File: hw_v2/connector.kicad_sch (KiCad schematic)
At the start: 22 parts, among them J1 Conn_02x24_Counter_Clockwise, J14 Conn_01x04, U11 L78M05ABDT-TR, U19 L78M05ABDT-TR, U25 74LVC2G17, U26 74LVC2G17, U8 AMS1117-3.3

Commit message: WIP v7
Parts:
- D37, U25: now in the parts list
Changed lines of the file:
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@@
 (kicad_sch
-	(version 20240101)
+	(version 20241004)
 	(generator "eeschema")
 	(generator_version "8.99")
@@
 		(shape input)
 		(at 264.16 82.55 0)
-		(fields_autoplaced yes)
 		(effects
 			(font
@@
 		(shape input)
 		(at 264.16 97.79 0)
-		(fields_autoplaced yes)
 		(effects
 			(font
@@
 		(shape input)
 		(at 264.16 90.17 0)
-		(fields_autoplaced yes)
 		(effects
 			(font
@@
 		(shape input)
 		(at 264.16 74.93 0)
-		(fields_autoplaced yes)
 		(effects
 			(font
@@
 		(unit 3)
 		(exclude_from_sim no)
-		(in_bom no)
+		(in_bom yes)
 		(on_board yes)
 		(dnp no)
@@
 		(at 149.86 40.005 0)
 		(unit 1)
-		(exclude_from_sim yes)
-		(in_bom no)
-		(on_board no)
+		(exclude_from_sim no)
+		(in_bom yes)
+		(on_board yes)
 		(dnp no)
 		(property "Reference" "#PWR0198"
@@
 		(at 143.51 34.29 270)
 		(unit 1)
-		(exclude_from_sim yes)
-		(in_bom no)
-		(on_board no)
+		(exclude_from_sim no)
+		(in_bom yes)
+		(on_board yes)
 		(dnp no)
 		(property "Reference" "D37"
@@
 		(at 251.46 82.55 0)
 		(unit 2)
-		(exclude_from_sim yes)
+		(exclude_from_sim no)
 		(in_bom yes)
 		(on_board yes)
@@
 		(at 143.51 22.225 0)
 		(unit 1)
-		(exclude_from_sim yes)
-		(in_bom no)
+		(exclude_from_sim no)
+		(in_bom yes)
 		(on_board yes)
 		(dnp no)
@@
 		(at 130.81 20.955 0)
 		(unit 1)
-		(exclude_from_sim yes)
-		(in_bom no)
-		(on_board no)
+		(exclude_from_sim no)
+		(in_bom yes)
+		(on_board yes)
 		(dnp no)
 		(property "Reference" "#PWR0199"

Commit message: hw v2
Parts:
- U26: footprint (none) -> Package_TO_SOT_SMD:SOT-363_SC-70-6
- U26: footprint (none) -> Package_TO_SOT_SMD:SOT-363_SC-70-6; now left out of the parts list
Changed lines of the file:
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@@
 			)
 		)
-		(property "Footprint" ""
+		(property "Footprint" "Package_TO_SOT_SMD:SOT-363_SC-70-6"
 			(at 250.19 147.32 0)
 			(effects
@@
 		(unit 1)
 		(exclude_from_sim no)
-		(in_bom yes)
+		(in_bom no)
 		(on_board yes)
 		(dnp no)
@@
 			)
 		)
-		(property "Footprint" ""
+		(property "Footprint" "Package_TO_SOT_SMD:SOT-363_SC-70-6"
 			(at 238.76 90.17 0)
 			(effects
@@
 			)
 		)
-		(property "Footprint" ""
+		(property "Footprint" "Package_TO_SOT_SMD:SOT-363_SC-70-6"
 			(at 251.46 97.79 0)
 			(effects

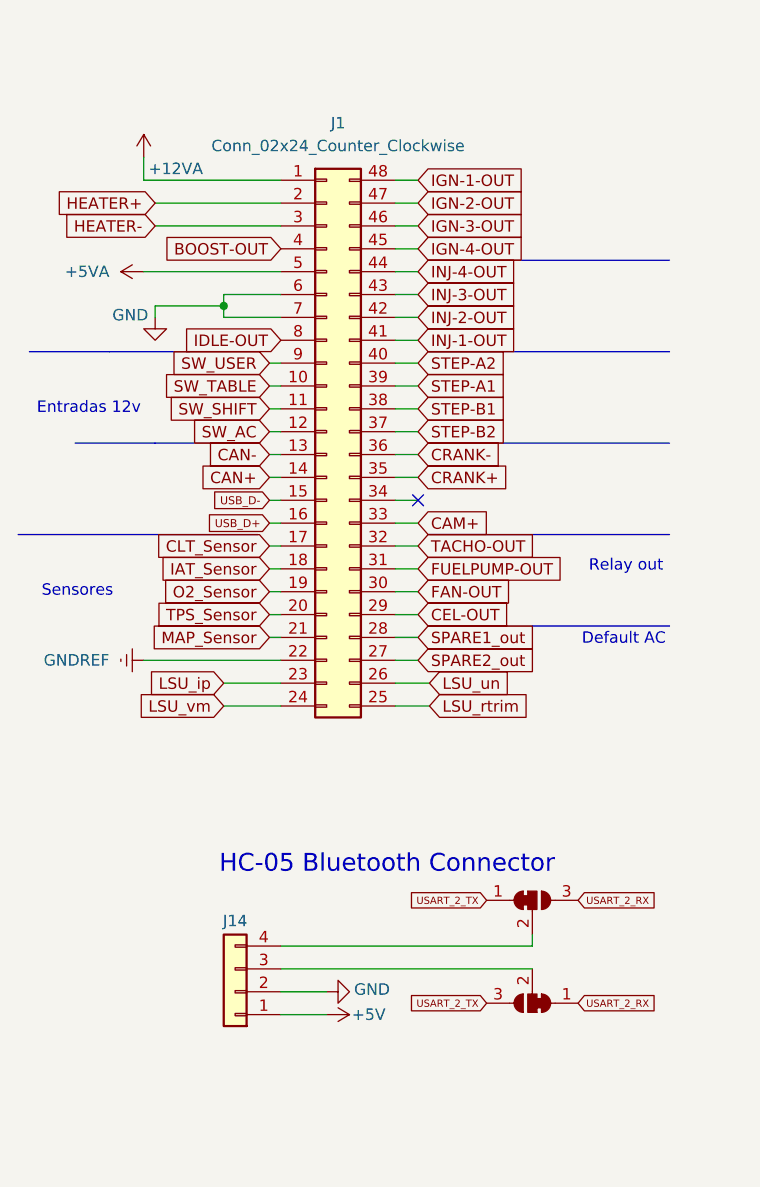
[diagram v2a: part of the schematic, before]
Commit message: fix LCSC codes
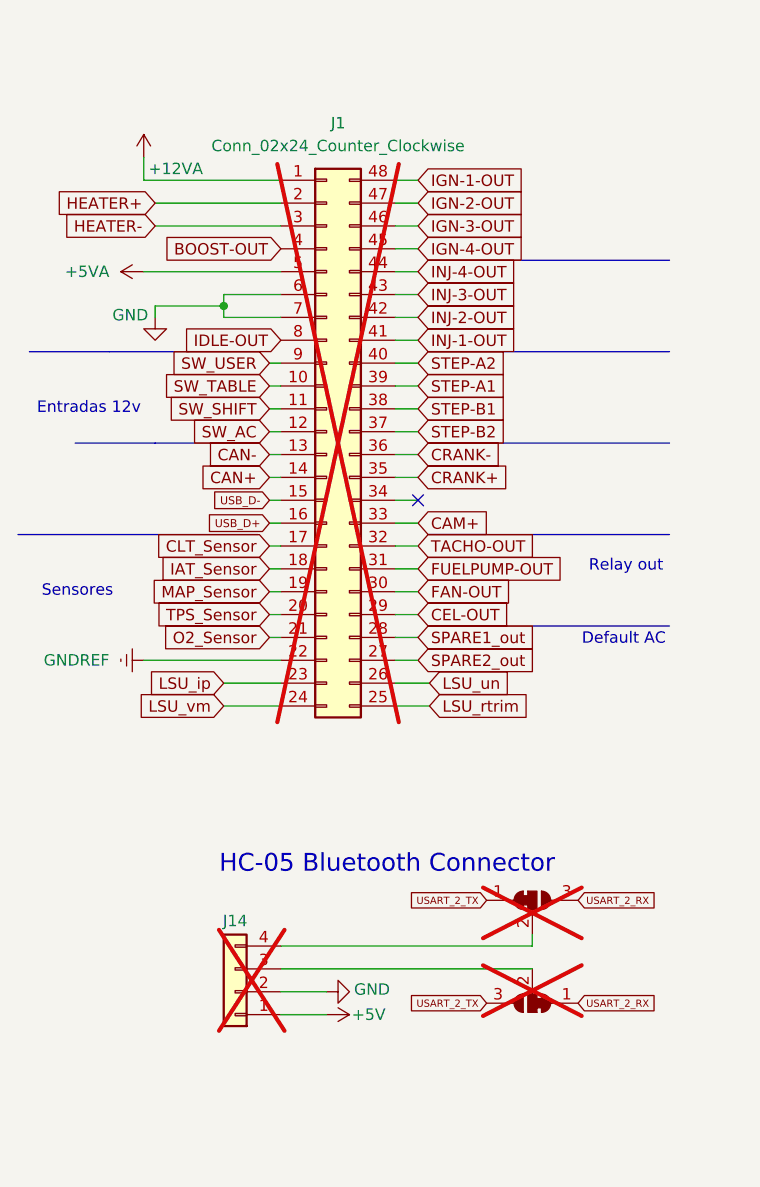
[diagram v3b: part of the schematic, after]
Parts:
- C51, C69, D17, RN7, U26: now in the parts list
- J1, JP10, JP9: now not fitted
- J14: now not fitted; now left out of the parts list
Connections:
- net MAP_Sensor: now also J1.19 (Pin_19); no longer J1.21 (Pin_21)
- net O2_Sensor: now also J1.21 (Pin_21); no longer J1.19 (Pin_19)
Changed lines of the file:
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@@
 	(global_label "MAP_Sensor"
 		(shape input)
-		(at 72.39 104.14 180)
+		(at 72.39 99.06 180)
 		(effects
 			(font
@@
 		)
 		(property "Intersheetrefs" "${INTERSHEET_REFS}"
-			(at 72.39 104.14 0)
+			(at 72.39 99.06 0)
 			(effects
 				(font
@@
 	(global_label "O2_Sensor"
 		(shape input)
-		(at 72.39 99.06 180)
+		(at 72.39 104.14 180)
 		(effects
 			(font
@@
 		)
 		(property "Intersheetrefs" "${INTERSHEET_REFS}"
-			(at 72.39 99.06 0)
+			(at 72.39 104.14 0)
 			(effects
 				(font
@@
 		(unit 3)
 		(exclude_from_sim no)
-		(in_bom no)
+		(in_bom yes)
 		(on_board yes)
 		(dnp no)
@@
 		(unit 1)
 		(exclude_from_sim no)
-		(in_bom no)
+		(in_bom yes)
 		(on_board yes)
 		(dnp no)
@@
 		(unit 1)
 		(exclude_from_sim no)
-		(in_bom no)
+		(in_bom yes)
 		(on_board yes)
 		(dnp no)
@@
 		(unit 1)
 		(exclude_from_sim no)
-		(in_bom no)
+		(in_bom yes)
 		(on_board yes)
 		(dnp no)
@@
 		(in_bom no)
 		(on_board yes)
-		(dnp no)
+		(dnp yes)
 		(property "Reference" "JP9"
 			(at 101.6 129.54 0)
@@
 		(unit 1)
 		(exclude_from_sim no)
-		(in_bom yes)
+		(in_bom no)
 		(on_board yes)
-		(dnp no)
+		(dnp yes)
 		(property "Reference" "J14"
 			(at 68.58 135.636 0)
@@
 		(in_bom no)
 		(on_board yes)
-		(dnp no)
+		(dnp yes)
 		(property "Reference" "J1"
 			(at 80.01 46.99 0)
@@
 		(in_bom no)
 		(on_board yes)
-		(dnp no)
+		(dnp yes)
 		(fields_autoplaced yes)
 		(property "Reference" "JP10"
@@
 		(unit 1)
 		(exclude_from_sim no)
-		(in_bom no)
+		(in_bom yes)
 		(on_board yes)
 		(dnp no)
@@
 		(unit 1)
 		(exclude_from_sim no)
-		(in_bom no)
+		(in_bom yes)
 		(on_board yes)
 		(dnp no)
@@
 		(unit 2)
 		(exclude_from_sim no)
-		(in_bom no)
+		(in_bom yes)
 		(on_board yes)
 		(dnp no)

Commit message: wip analog frontend & power
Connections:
- net BOOST-OUT: now also J1.8 (Pin_8); no longer J1.4 (Pin_4)
- net IDLE-OUT: now also J1.4 (Pin_4); no longer J1.8 (Pin_8)
- net MAP_Sensor: now also J1.20 (Pin_20); no longer J1.19 (Pin_19)
- net TPS_Sensor: now also J1.19 (Pin_19); no longer J1.20 (Pin_20)

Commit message: wip analog frontend & power
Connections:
- net SW_AC: now also RN7.5 (R4.2); no longer RN7.8 (R1.2)
- net SW_SHIFT: now also RN7.6 (R3.2); no longer RN7.7 (R2.2)
- net SW_TABLE: now also RN7.7 (R2.2); no longer RN7.6 (R3.2)
- net SW_USER: now also RN7.8 (R1.2); no longer RN7.5 (R4.2)
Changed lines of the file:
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@@
+	)
+	(junction
+		(at 214.63 97.79)
+		(diameter 0)
+		(color 0 0 0 0)
 	)
 	(junction
@@
 	)
 	(junction
+		(at 219.71 82.55)
+		(diameter 0)
+		(color 0 0 0 0)
+	)
+	(junction
 		(at 209.55 27.94)
 		(diameter 0)
@@
 	)
 	(junction
+		(at 222.25 74.93)
+		(diameter 0)
+		(color 0 0 0 0)
+	)
+	(junction
 		(at 217.17 90.17)
 		(diameter 0)
@@
 	)
 	(junction
-		(at 219.71 90.17)
-		(diameter 0)
-		(color 0 0 0 0)
-	)
-	(junction
-		(at 217.17 82.55)
-		(diameter 0)
-		(color 0 0 0 0)
-	)
-	(junction
 		(at 212.09 82.55)
-		(diameter 0)
-		(color 0 0 0 0)
-	)
-	(junction
-		(at 214.63 74.93)
 		(diameter 0)
 		(color 0 0 0 0)
@@
 	(wire
 		(pts
+			(xy 219.71 69.85) (xy 219.71 82.55)
+		)
+		(stroke
+			(width 0)
+			(type default)
+		)
+	)
+	(wire
+		(pts
 			(xy 217.17 114.3) (xy 217.17 111.76)
 		)
@@
 	(wire
 		(pts
+			(xy 212.09 82.55) (xy 219.71 82.55)
+		)
+		(stroke
+			(width 0)
+			(type default)
+		)
+	)
+	(wire
+		(pts
+			(xy 217.17 69.85) (xy 217.17 90.17)
+		)
+		(stroke
+			(width 0)
+			(type default)
+		)
+	)
+	(wire
+		(pts
 			(xy 195.58 31.75) (xy 195.58 30.48)
 		)
@@
 	(wire
 		(pts
-			(xy 219.71 90.17) (xy 223.52 90.17)
+			(xy 217.17 90.17) (xy 223.52 90.17)
 		)
 		(stroke
@@
 	(wire
 		(pts
+			(xy 214.63 69.85) (xy 214.63 97.79)
+		)
+		(stroke
+			(width 0)
+			(type default)
+		)
+	)
+	(wire
+		(pts
 			(xy 72.39 73.66) (xy 73.66 73.66)
 		)
@@
 	(wire
 		(pts
-			(xy 212.09 82.55) (xy 217.17 82.55)
-		)
-		(stroke
-			(width 0)
-			(type default)
-		)
-	)
-	(wire
-		(pts
 			(xy 222.25 35.56) (xy 222.25 39.37)
 		)
@@
 	(wire
 		(pts
+			(xy 222.25 74.93) (xy 223.52 74.93)
+		)
+		(stroke
+			(width 0)
+			(type default)
+		)
+	)
+	(wire
+		(pts
 			(xy 143.51 24.765) (xy 143.51 27.305)
 		)
@@
 	(wire
 		(pts
-			(xy 217.17 82.55) (xy 236.22 82.55)
-		)
-		(stroke
-			(width 0)
-			(type default)
-		)
-	)
-	(wire
-		(pts
 			(xy 217.17 57.15) (xy 219.71 57.15)
 		)
@@
 	(wire
 		(pts
-			(xy 219.71 69.85) (xy 219.71 90.17)
-		)
-		(stroke
-			(width 0)
-			(type default)
-		)
-	)
-	(wire
-		(pts
 			(xy 59.69 55.88) (xy 73.66 55.88)
 		)
@@
 		)
 	)
+	(wire
+		(pts
+			(xy 214.63 97.79) (xy 222.25 97.79)
+		)
+		(stroke
+			(width 0)
+			(type default)
+		)
+	)
 	(polyline
 		(pts
@@
 	(wire
 		(pts
-			(xy 214.63 69.85) (xy 214.63 74.93)
-		)
-		(stroke
-			(width 0)
-			(type default)
-		)
-	)
-	(wire
-		(pts
 			(xy 88.9 55.88) (xy 86.36 55.88)
 		)
@@
 		)
 	)
-	(wire
-		(pts
-			(xy 222.25 69.85) (xy 222.25 97.79)
-		)
-		(stroke
-			(width 0)
-			(type default)
-		)
-	)
 	(polyline
 		(pts
@@
 	(wire
 		(pts
+			(xy 222.25 69.85) (xy 222.25 74.93)
+		)
+		(stroke
+			(width 0)
+			(type default)
+		)
+	)
+	(wire
+		(pts
 			(xy 271.78 35.56) (xy 271.78 38.1)
 		)
@@
 	(wire
 		(pts
+			(xy 219.71 82.55) (xy 236.22 82.55)
+		)
+		(stroke
+			(width 0)
+			(type default)
+		)
+	)
+	(wire
+		(pts
 			(xy 143.51 40.005) (xy 143.51 38.1)
 		)
@@
 	(wire
 		(pts
-			(xy 207.01 74.93) (xy 214.63 74.93)
-		)
-		(stroke
-			(width 0)
-			(type default)
-		)
-	)
-	(wire
-		(pts
-			(xy 204.47 97.79) (xy 222.25 97.79)
-		)
-		(stroke
-			(width 0)
-			(type default)
-		)
-	)
-	(wire
-		(pts
-			(xy 214.63 74.93) (xy 223.52 74.93)
+			(xy 207.01 74.93) (xy 222.25 74.93)
+		)
+		(stroke
+			(width 0)
+			(type default)
+		)
+	)
+	(wire
+		(pts
+			(xy 204.47 97.79) (xy 214.63 97.79)
 		)
 		(stroke
@@
 	(wire
 		(pts
-			(xy 217.17 90.17) (xy 219.71 90.17)
-		)
-		(stroke
-			(width 0)
-			(type default)
-		)
-	)
-	(wire
-		(pts
 			(xy 222.25 111.76) (xy 222.25 107.95)
 		)
@@
 		)
 		(stroke
-			(width 0)
-			(type default)
-		)
-	)
-	(wire
-		(pts
-			(xy 217.17 69.85) (xy 217.17 82.55)
-		)
-		(stroke

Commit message: Fix some ERC errors
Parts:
- C69: symbol Device:CP_Small -> Device:C_Polarized_Small
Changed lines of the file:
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@@
 			)
 		)
-		(property "Description" ""
+		(property "Description" "Power symbol creates a global label with name \"GND\" , ground"
 			(at 262.89 157.48 0)
 			(effects
@@
 	)
 	(symbol
-		(lib_id "Device:CP_Small")
+		(lib_id "Device:C_Polarized_Small")
 		(at 149.86 33.655 0)
 		(unit 1)
@@
 			)
 		)
-		(property "Description" ""
+		(property "Description" "Polarized capacitor, small symbol"
 			(at 149.86 33.655 0)
 			(effects
@@
 			)
 		)
-		(property "Description" ""
+		(property "Description" "Power symbol creates a global label with name \"GND\" , ground"
 			(at 184.15 40.64 0)
 			(effects
@@
 			)
 		)
-		(property "Description" ""
+		(property "Description" "Power symbol creates a global label with name \"GND\" , ground"
 			(at 232.41 39.37 0)
 			(effects
@@
 			)
 		)
-		(property "Description" ""
+		(property "Description" "Power symbol creates a global label with name \"GND\" , ground"
 			(at 149.86 40.005 0)
 			(effects
@@
 			)
 		)
-		(property "Description" ""
+		(property "Description" "Power symbol creates a global label with name \"+3V3\""
 			(at 195.58 27.94 0)
 			(effects
@@
 			)
 		)
-		(property "Description" ""
+		(property "Description" "Power symbol creates a global label with name \"+3V3\""
 			(at 250.19 137.16 0)
 			(effects
@@
 			)
 		)
-		(property "Description" ""
+		(property "Description" "Power symbol creates a global label with name \"GND\" , ground"
 			(at 195.58 39.37 0)
 			(effects
@@
 			)
 		)
-		(property "Description" ""
+		(property "Description" "Power symbol creates a global label with name \"GND\" , ground"
 			(at 143.51 40.005 0)
 			(effects
@@
 			)
 		)
-		(property "Description" ""
+		(property "Description" "Power symbol creates a global label with name \"GND\" , ground"
 			(at 261.62 38.1 0)
 			(effects
@@
 			)
 		)
-		(property "Description" ""
+		(property "Description" "Power symbol creates a global label with name \"GND\" , ground"
 			(at 217.17 114.3 0)
 			(effects
@@
 			)
 		)
-		(property "Description" ""
+		(property "Description" "Power symbol creates a global label with name \"GND\" , ground"
 			(at 59.69 68.58 0)
 			(effects
@@
 			)
 		)
-		(property "Description" ""
+		(property "Description" "Power symbol creates a global label with name \"GND\" , ground"
 			(at 271.78 38.1 0)
 			(effects
@@
 			)
 		)
-		(property "Description" ""
+		(property "Description" "Power symbol creates a global label with name \"GND\" , ground"
 			(at 250.19 157.48 0)
 			(effects
@@
 			)
 		)
-		(property "Description" ""
+		(property "Description" "Power symbol creates a global label with name \"GND\" , ground"
 			(at 248.92 38.1 0)
 			(effects
@@
 			)
 		)
-		(property "Description" ""
+		(property "Description" "Power symbol creates a global label with name \"GND\" , ground"
 			(at 222.25 39.37 0)
 			(effects
@@
 			)
 		)
-		(property "Description" ""
+		(property "Description" "Power symbol creates a global label with name \"+3V3\""
 			(at 262.89 137.16 0)
 			(effects
@@
 			)
 		)
-		(property "Description" ""
+		(property "Description" "Power symbol creates a global label with name \"+5V\""
 			(at 172.72 29.21 0)
 			(effects
@@
 			)
 		)
-		(property "Description" ""
+		(property "Description" "Power symbol creates a global label with name \"GND\" , ground"
 			(at 209.55 39.37 0)
 			(effects
@@
 			)
 		)
-		(property "Description" ""
+		(property "Description" "Power symbol creates a global label with name \"GND\" , ground"
 			(at 78.74 143.51 0)
 			(effects

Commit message: planito mas catolico
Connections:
- net GNDREF is gone; now on net GND: J1.22 (Pin_22)
- net CAM+: now also J1.34 (Pin_34); no longer J1.33 (Pin_33)
- net FUELPUMP-OUT: now also J1.32 (Pin_32); no longer J1.31 (Pin_31)
- net TACHO-OUT: now also J1.33 (Pin_33); no longer J1.32 (Pin_32)
- net SPARE1_out: no longer names the net of J1.28 (Pin_28)
- net SPARE2_out: no longer names the net of J1.27 (Pin_27)
- net STEP-A1 renamed STEPPER-A2
- net STEP-A2 renamed STEPPER-A1
- net STEP-B1 renamed STEPPER-B1
- net STEP-B2 renamed STEPPER-B2
- new net FAN2-OUT: J1.31 (Pin_31)
- no-connect marks 1 -> 2
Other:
- moved on the sheet: C69, D17
